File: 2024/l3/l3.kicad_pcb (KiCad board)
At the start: 2 copper layers, 137.5 x 129.1 mm, 23 parts, among them J1 Conn_01x04, SW1 SW_SPDT, SW2 SW_SPDT, SW3 SW_SPDT, SW4 SW_SPDT, U4 DEV-15583

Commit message: final 0.9
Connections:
- net /SCLToF renamed SCLToF
- net /SDAToF renamed SDAToF
- net /XSHUT1 renamed XSHUT1
- net /XSHUT2 renamed XSHUT2
- net /XSHUT3 renamed XSHUT3
- net /XSHUT4 renamed XSHUT4

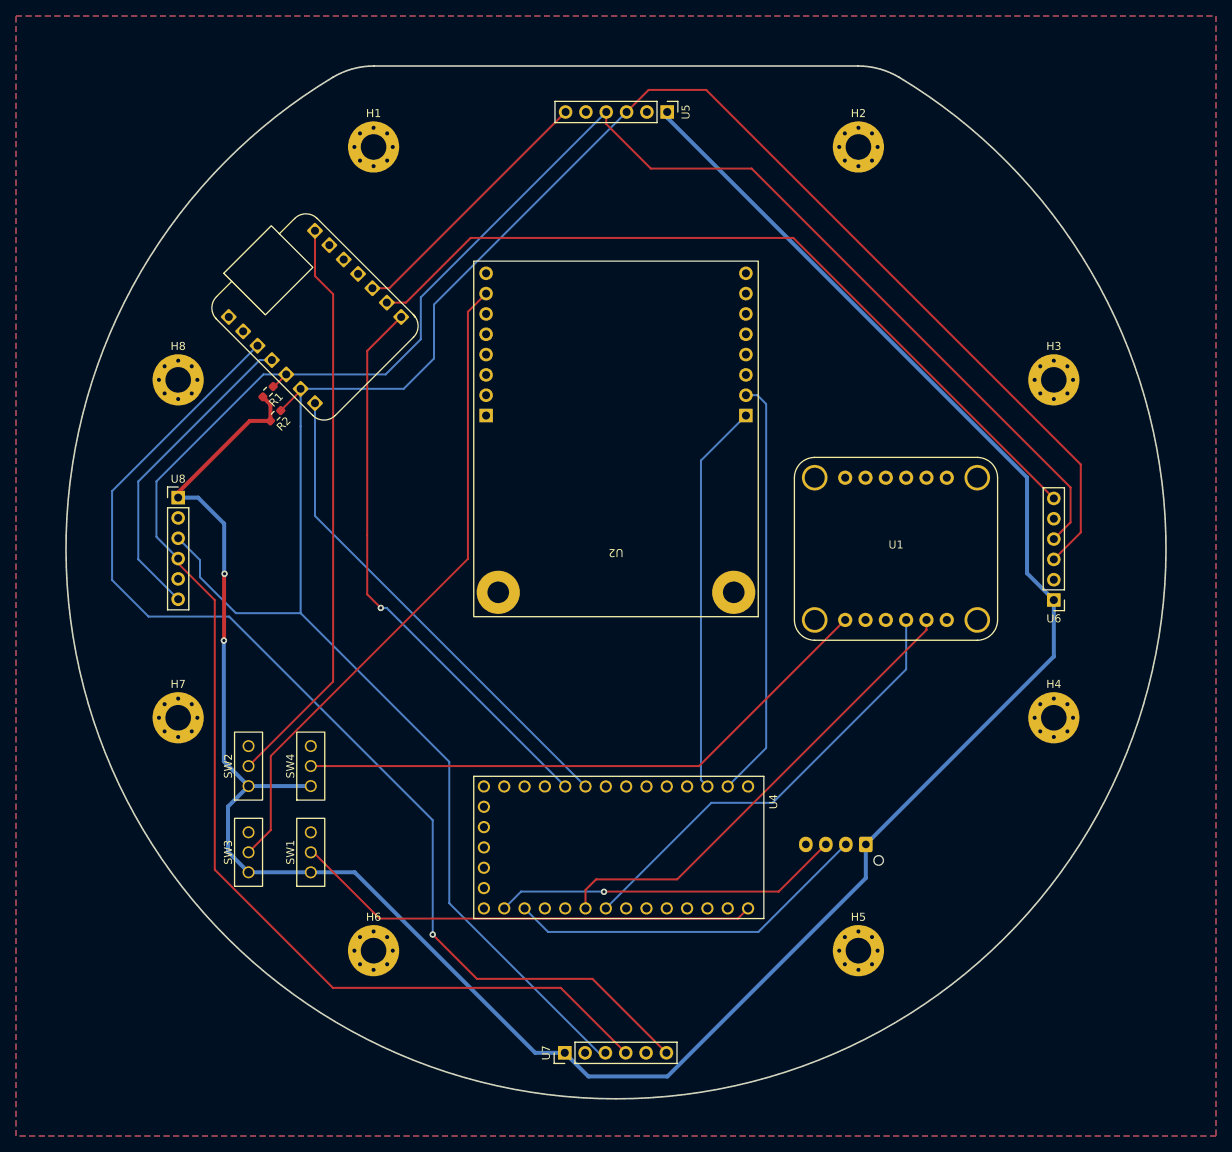
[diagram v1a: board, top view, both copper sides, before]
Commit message: tf luna
gerber created for l1 and l2
l3 changed the tof from vl53l1x to tf luna
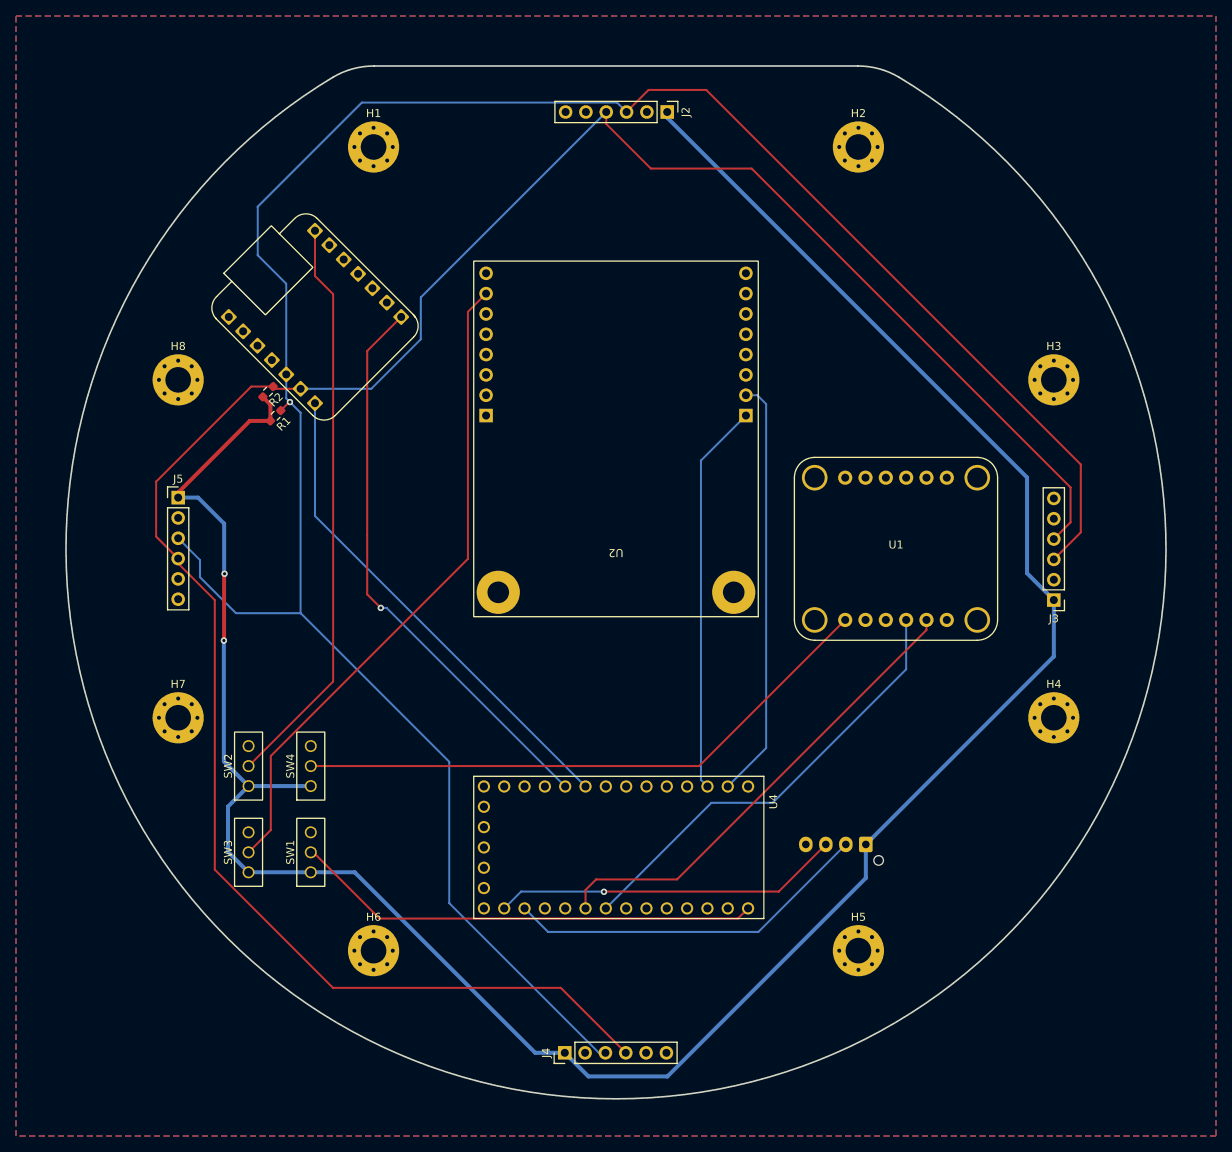
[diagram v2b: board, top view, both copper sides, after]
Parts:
- J2: renamed from U5; value ~ -> Conn_01x06
- J3: renamed from U6; value ~ -> Conn_01x06
- J4: renamed from U7; value ~ -> Conn_01x06
- J5: renamed from U8; value ~ -> Conn_01x06
- renumbered R2 to R1, R1 to R2
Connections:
- J2 pad 2: GND -> unconnected-(J2-Pin_2-Pad2)
- J2 pad 3: SCLToF -> SDAToF
- J2 pad 4: SDAToF -> SCLToF
- J2 pad 5: unconnected-(U5-GPIO1-Pad5) -> GND
- J2 pad 6: XSHUT1 -> unconnected-(J2-Pin_6-Pad6)
- J3 pad 2: GND -> unconnected-(J3-Pin_2-Pad2)
- J3 pad 3: SCLToF -> SDAToF
- J3 pad 4: SDAToF -> SCLToF
- J3 pad 5: unconnected-(U6-GPIO1-Pad5) -> GND
- J3 pad 6: XSHUT2 -> unconnected-(J3-Pin_6-Pad6)
- J4 pad 2: GND -> unconnected-(J4-Pin_2-Pad2)
- J4 pad 3: SCLToF -> SDAToF
- J4 pad 4: SDAToF -> SCLToF
- J4 pad 5: unconnected-(U7-GPIO1-Pad5) -> GND
- J4 pad 6: XSHUT3 -> unconnected-(J4-Pin_6-Pad6)
- J5 pad 2: GND -> unconnected-(J5-Pin_2-Pad2)
- J5 pad 3: SCLToF -> SDAToF
- J5 pad 4: SDAToF -> SCLToF
- J5 pad 5: unconnected-(U8-GPIO1-Pad5) -> GND
- J5 pad 6: XSHUT4 -> unconnected-(J5-Pin_6-Pad6)
- R1 pad 1: SCLToF -> SDAToF
- R2 pad 1: SDAToF -> SCLToF
- U3 pad 2: XSHUT3 -> unconnected-(U3-D2-Pad2)
- U3 pad 3: XSHUT4 -> unconnected-(U3-D3-Pad3)
- U3 pad 8: XSHUT2 -> unconnected-(U3-D8-Pad8)
- U3 pad 9: XSHUT1 -> unconnected-(U3-D9-Pad9)
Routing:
- net XSHUT3: track 139.0 -> 0.00 mm, vias 1 -> 0
- net XSHUT2: track 100.2 -> 0.00 mm
- net XSHUT4: track 39.8 -> 0.00 mm
- net XSHUT1: track 33.3 -> 0.00 mm
- net SDAToF: track 278.8 -> 288.8 mm, vias 0 -> 1
- net SCLToF: track 273.3 -> 277.1 mm

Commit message: tf luna mount complete
adjusted a lot of stuff
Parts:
- moved J4 24.6 mm to (98.6, 135.0)
- moved J2 16.6 mm to (111.4, 58.6)
- moved J5 15.3 mm to (65.5, 90.2)
- moved U4 10.3 mm to (105.0, 123.6)
- moved J3 7.50 mm to (152.2, 103.0)
- moved U1 3.16 mm to (136.8, 96.7)
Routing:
- net SDAToF: track 288.8 -> 233.3 mm
- net +5V: track 305.0 -> 265.6 mm
- net SCLToF: track 277.1 -> 258.5 mm
- net /RXCam: track 52.8 -> 42.3 mm
- net /TXCam: track 49.0 -> 38.7 mm
- net /TXToF: track 61.9 -> 54.7 mm
- net /SCLComp: track 56.1 -> 50.5 mm
- net /SDAComp: track 59.6 -> 54.0 mm
- net /RXToF: track 71.1 -> 66.9 mm
- net /RXL2: track 45.9 -> 42.2 mm
- net /TeensySwitch: track 58.6 -> 56.0 mm
- net /CompassSwitch: track 74.4 -> 73.0 mm
- net /TXL2: track 43.5 -> 42.9 mm

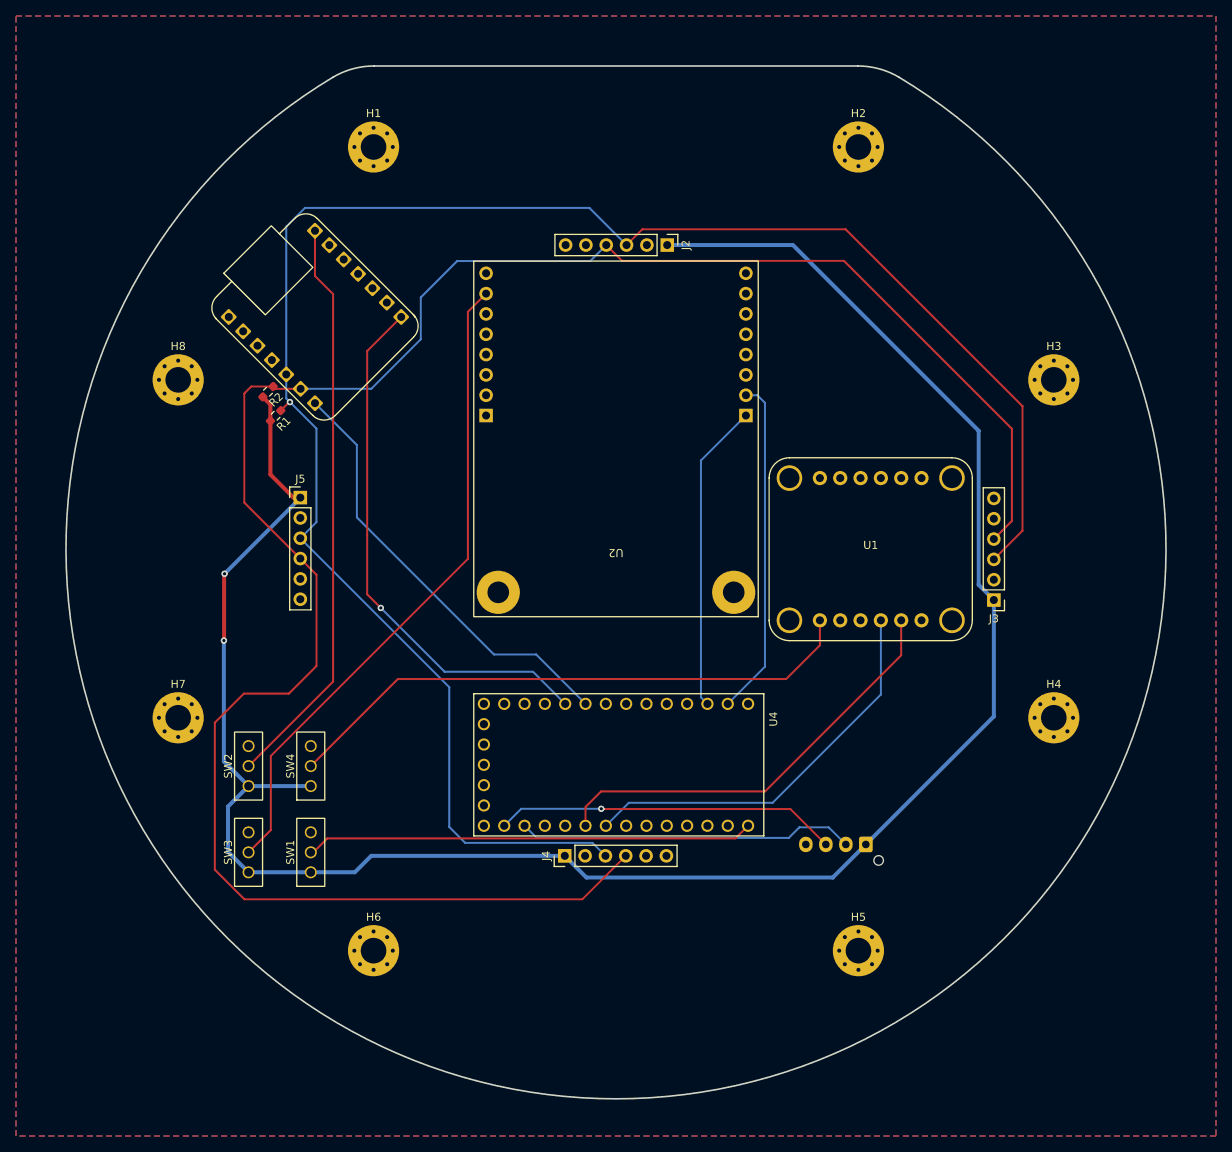
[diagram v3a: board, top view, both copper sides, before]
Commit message: final 0.92
l3 traces going from the switch to vin of components 0.5mm just to be sure
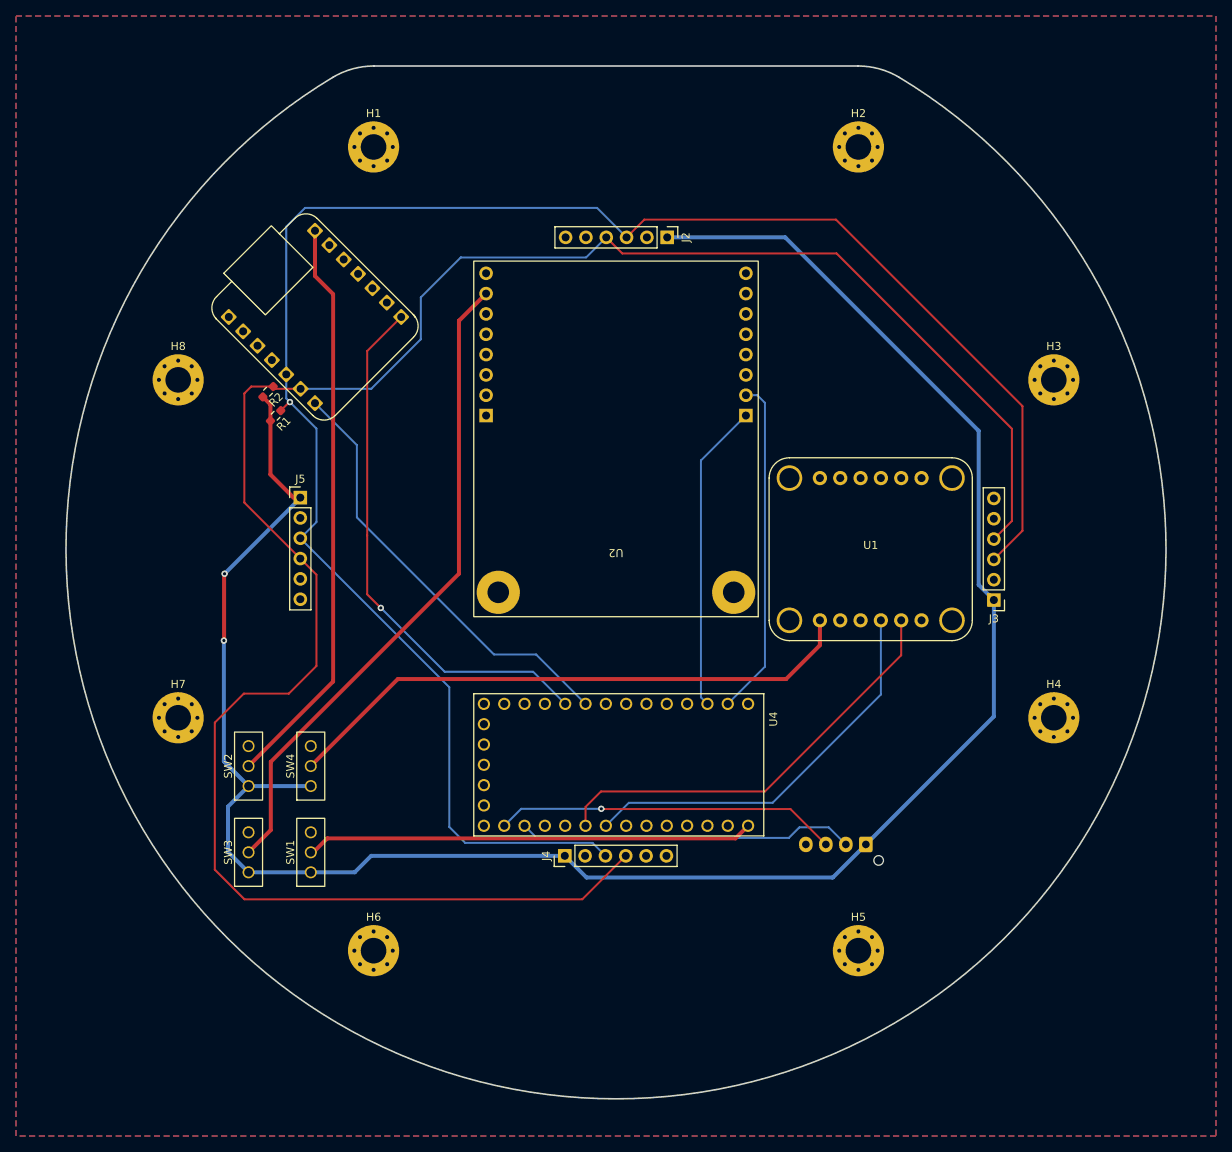
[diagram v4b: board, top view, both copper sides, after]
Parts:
- moved J2 0.96 mm to (111.4, 57.7)
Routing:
- net SCLToF: track 258.5 -> 259.3 mm
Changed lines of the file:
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@@
 	(footprint "Connector_PinHeader_2.54mm:PinHeader_1x06_P2.54mm_Vertical"
 		(layer "F.Cu")
-		(at 111.4 58.63 -90)
+		(at 111.4 57.67 -90)
 		(descr "Through hole straight pin header, 1x06, 2.54mm pitch, single row")
 		(tags "Through hole pin header THT 1x06 2.54mm single row")
@@
 	)
 	(segment
-		(start 65.54 90.202548)
-		(end 65.54 90.25)
+		(start 150.33 101.102548)
+		(end 150.33 81.85)
 		(width 0.5)
 		(layer "B.Cu")
@@
 	)
 	(segment
-		(start 55.99 108.07)
-		(end 55.98 108.08)
+		(start 65.54 90.202548)
+		(end 65.54 90.25)
 		(width 0.5)
 		(layer "B.Cu")
@@
 	)
 	(segment
-		(start 150.33 101.102548)
-		(end 152.23 103.002548)
+		(start 55.99 108.07)
+		(end 55.98 108.08)
 		(width 0.5)
 		(layer "B.Cu")
@@
 	)
 	(segment
-		(start 127.11 58.63)
-		(end 150.33 81.85)
-		(width 0.5)
-		(layer "B.Cu")
-		(net 3)
-	)
-	(segment
 		(start 56.5 128.83)
 		(end 59.07 126.26)
@@
 	)
 	(segment
-		(start 127.11 58.63)
-		(end 111.4 58.63)
-		(width 0.5)
-		(layer "B.Cu")
-		(net 3)
-	)
-	(segment
 		(start 136.23 133.555)
 		(end 132.095 137.69)
@@
 	)
 	(segment
-		(start 150.33 81.85)
-		(end 150.33 101.102548)
-		(width 0.5)
-		(layer "B.Cu")
-		(net 3)
-	)
-	(segment
 		(start 59.07 137.04)
 		(end 56.5 134.47)
@@
 	)
 	(segment
+		(start 126.15 57.67)
+		(end 111.4 57.67)
+		(width 0.5)
+		(layer "B.Cu")
+		(net 3)
+	)
+	(segment
 		(start 74.4 134.98)
 		(end 98.6 134.98)
@@
 	)
 	(segment
+		(start 152.23 103.002548)
+		(end 150.33 101.102548)
+		(width 0.5)
+		(layer "B.Cu")
+		(net 3)
+	)
+	(segment
+		(start 150.33 81.85)
+		(end 126.15 57.67)
+		(width 0.5)
+		(layer "B.Cu")
+		(net 3)
+	)
+	(segment
 		(start 131.23 133.555)
 		(end 126.805 129.13)
@@
 	)
 	(segment
+		(start 105.79 59.68)
+		(end 132.57 59.68)
+		(width 0.25)
+		(layer "F.Cu")
+		(net 5)
+	)
+	(segment
 		(start 65.54 97.822548)
 		(end 67.56 99.842548)
@@
 	)
 	(segment
-		(start 133.5 60.61)
-		(end 154.49 81.6)
+		(start 154.49 81.6)
+		(end 154.49 93.122548)
 		(width 0.25)
 		(layer "F.Cu")
@@
 	)
 	(segment
+		(start 103.78 57.67)
+		(end 105.79 59.68)
+		(width 0.25)
+		(layer "F.Cu")
+		(net 5)
+	)
+	(segment
 		(start 67.56 111.24972)
 		(end 64.10972 114.7)
@@
 	)
 	(segment
-		(start 103.78 58.63)
-		(end 105.76 60.61)
+		(start 132.57 59.68)
+		(end 154.49 81.6)
 		(width 0.25)
 		(layer "F.Cu")
@@
 	)
 	(segment
-		(start 105.76 60.61)
-		(end 133.5 60.61)
-		(width 0.25)
-		(layer "F.Cu")
-		(net 5)
-	)
-	(segment
 		(start 62.145235 76.316765)
 		(end 59.403235 76.316765)
@@
 	)
 	(segment
-		(start 154.49 81.6)
-		(end 154.49 93.122548)
+		(start 154.49 93.122548)
+		(end 152.23 95.382548)
 		(width 0.25)
 		(layer "F.Cu")
@@
 	)
 	(segment
-		(start 154.49 93.122548)
-		(end 152.23 95.382548)
-		(width 0.25)
-		(layer "F.Cu")
-		(net 5)
-	)
-	(segment
 		(start 62.145235 76.316765)
 		(end 62.269031 76.316765)
@@
 	)
 	(segment
-		(start 74.409744 76.600256)
-		(end 65.577642 76.600256)
+		(start 80.6 65.179548)
+		(end 80.6 70.41)
 		(width 0.25)
 		(layer "B.Cu")
@@
 	)
 	(segment
-		(start 80.6 70.41)
-		(end 74.409744 76.600256)
+		(start 85.599548 60.18)
+		(end 80.6 65.179548)
 		(width 0.25)
 		(layer "B.Cu")
@@
 	)
 	(segment
-		(start 85.149548 60.63)
-		(end 80.6 65.179548)
+		(start 101.27 60.18)
+		(end 85.599548 60.18)
 		(width 0.25)
 		(layer "B.Cu")
@@
 	)
 	(segment
-		(start 103.78 58.63)
-		(end 101.78 60.63)
+		(start 74.409744 76.600256)
+		(end 65.577642 76.600256)
 		(width 0.25)
 		(layer "B.Cu")
@@
 	)
 	(segment
-		(start 101.78 60.63)
-		(end 85.149548 60.63)
+		(start 80.6 70.41)
+		(end 74.409744 76.600256)
 		(width 0.25)
 		(layer "B.Cu")
@@
 	)
 	(segment
-		(start 80.6 65.179548)
-		(end 80.6 70.41)
+		(start 103.78 57.67)
+		(end 101.27 60.18)
 		(width 0.25)
 		(layer "B.Cu")
@@
 		(start 67.17 134.54)
 		(end 68.91 132.8)
-		(width 0.25)
+		(width 0.5)
 		(layer "F.Cu")
 		(net 6)
@@
 		(start 68.91 132.8)
 		(end 119.932548 132.8)
-		(width 0.25)
+		(width 0.5)
 		(layer "F.Cu")
 		(net 6)
@@
 		(start 119.932548 132.8)
 		(end 121.51 131.222548)
-		(width 0.25)
+		(width 0.5)
 		(layer "F.Cu")
 		(net 6)
@@
 		(start 130.49 108.652548)
 		(end 130.49 105.54)
-		(width 0.25)
+		(width 0.5)
 		(layer "F.Cu")
 		(net 11)
@@
 		(start 77.73 112.88)
 		(end 126.262548 112.88)
-		(width 0.25)
+		(width 0.5)
 		(layer "F.Cu")
 		(net 11)
@@
 		(start 126.262548 112.88)
 		(end 130.49 108.652548)
-		(width 0.25)
+		(width 0.5)
 		(layer "F.Cu")
 		(net 11)
@@
 		(start 66.85 123.76)
 		(end 77.73 112.88)
-		(width 0.25)
+		(width 0.5)
 		(layer "F.Cu")
 		(net 11)
@@
 	)
 	(segment
-		(start 86.49 66.972548)
+		(start 85.37 68.092548)
 		(end 88.761 64.701548)
-		(width 0.25)
+		(width 0.5)
 		(layer "F.Cu")
 		(net 23)
 	)
 	(segment
-		(start 61.85 131.76)
-		(end 61.85 122.50028)
-		(width 0.25)
+		(start 85.37 99.71)
+		(end 85.37 68.092548)
+		(width 0.5)
 		(layer "F.Cu")
 		(net 23)
 	)
 	(segment
-		(start 86.49 97.86028)
-		(end 86.49 66.972548)
-		(width 0.25)
+		(start 61.85 131.76)
+		(end 61.85 123.23)
+		(width 0.5)
 		(layer "F.Cu")
 		(net 23)
@@
 		(start 59.07 134.54)
 		(end 61.85 131.76)
-		(width 0.25)
+		(width 0.5)
 		(layer "F.Cu")
 		(net 23)
 	)
 	(segment
-		(start 61.85 122.50028)
-		(end 86.49 97.86028)
-		(width 0.25)
+		(start 61.85 123.23)
+		(end 85.37 99.71)
+		(width 0.5)
 		(layer "F.Cu")
 		(net 23)
@@
 		(start 59.07 123.76)
 		(end 69.639328 113.190672)
-		(width 0.25)
+		(width 0.5)
 		(layer "F.Cu")
 		(net 34)
@@
 		(start 69.639328 113.190672)
 		(end 69.639328 64.769328)
-		(width 0.25)
+		(width 0.5)
 		(layer "F.Cu")
 		(net 34)
@@
 		(start 69.639328 64.769328)
 		(end 67.373693 62.503693)
-		(width 0.25)
+		(width 0.5)
 		(layer "F.Cu")
 		(net 34)
@@
 		(start 67.373693 62.503693)
 		(end 67.373693 56.843693)
-		(width 0.25)
+		(width 0.5)
 		(layer "F.Cu")
 		(net 34)
@@
 	)
 	(segment
-		(start 133.7 56.66)
-		(end 155.81 78.77)
+		(start 63.095235 79.324765)
+		(end 64.16 78.26)
 		(width 0.25)
 		(layer "F.Cu")
@@
 	)
 	(segment
-		(start 63.095235 79.324765)
-		(end 64.16 78.26)
+		(start 64.16 78.26)
+		(end 64.24 78.26)
 		(width 0.25)
 		(layer "F.Cu")
@@
 	)
 	(segment
-		(start 155.81 94.342548)
-		(end 152.23 97.922548)
+		(start 108.54 55.45)
+		(end 106.32 57.67)
 		(width 0.25)
 		(layer "F.Cu")
@@
 	)
 	(segment
-		(start 64.16 78.26)
-		(end 64.24 78.26)
+		(start 155.81 94.342548)
+		(end 155.81 78.77)
 		(width 0.25)
 		(layer "F.Cu")
@@
 	)
 	(segment
-		(start 106.32 58.63)
-		(end 108.29 56.66)
+		(start 152.23 97.922548)
+		(end 155.81 94.342548)
 		(width 0.25)
 		(layer "F.Cu")
@@
 	(segment
 		(start 155.81 78.77)
-		(end 155.81 94.342548)
+		(end 132.49 55.45)
 		(width 0.25)
 		(layer "F.Cu")
@@
 	)
 	(segment
-		(start 108.29 56.66)
-		(end 133.7 56.66)
+		(start 132.49 55.45)
+		(end 108.54 55.45)
 		(width 0.25)
 		(layer "F.Cu")
@@
 	)
 	(segment
-		(start 66.12 53.99)
-		(end 63.781591 56.328409)
+		(start 67.555 93.267548)
+		(end 65.54 95.282548)
 		(width 0.25)
 		(layer "B.Cu")
@@
 	)
 	(segment
-		(start 67.555 93.267548)
-		(end 65.54 95.282548)
+		(start 63.781591 74.804205)
+		(end 63.781591 56.328409)
 		(width 0.25)
 		(layer "B.Cu")
@@
 	)
 	(segment
-		(start 63.781591 56.328409)
-		(end 63.781591 74.804205)
+		(start 66.12 53.99)
+		(end 102.64 53.99)
 		(width 0.25)
 		(layer "B.Cu")
@@
 	)
 	(segment
-		(start 106.32 58.63)
-		(end 101.68 53.99)
+		(start 102.64 53.99)
+		(end 106.32 57.67)
 		(width 0.25)
 		(layer "B.Cu")
@@
 	)
 	(segment
-		(start 101.68 53.99)
-		(end 66.12 53.99)
+		(start 65.54 95.282548)
+		(end 84.16 113.902548)
 		(width 0.25)
 		(layer "B.Cu")
@@
 	)
 	(segment
-		(start 65.54 95.282548)
-		(end 84.16 113.902548)
+		(start 63.781591 56.328409)
+		(end 66.12 53.99)
 		(width 0.25)
 		(layer "B.Cu")
